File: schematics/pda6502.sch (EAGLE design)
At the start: 32 parts, among them IC1 74HC00D, IC2 74HC138D, IC3 DS1813-SMD, J1 CON_HEADER_2X07-PTH, U1 W65C02S, U2 W65C22S, U3 28C256, U4 UM61256AK-12

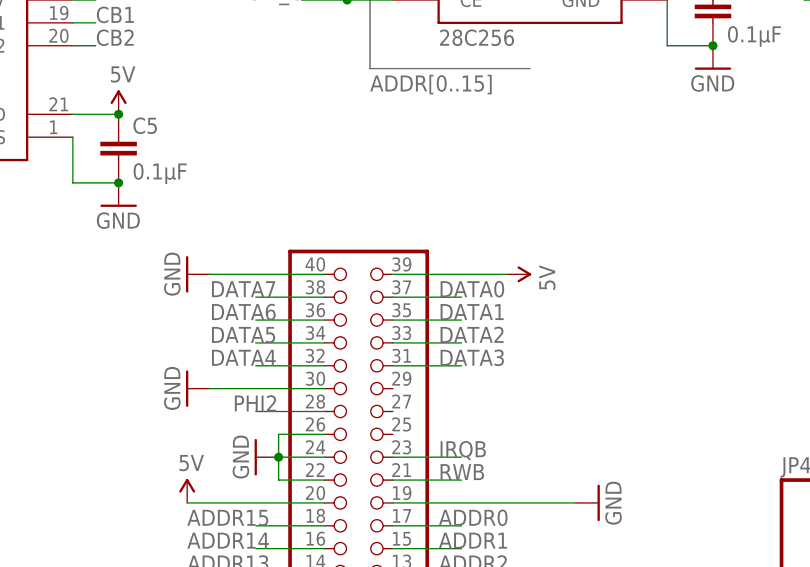
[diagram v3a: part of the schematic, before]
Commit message: schematics: ERC fixes; expansion header has decoupling cap.
(Does the cap even make sense there? The more the merrier...)
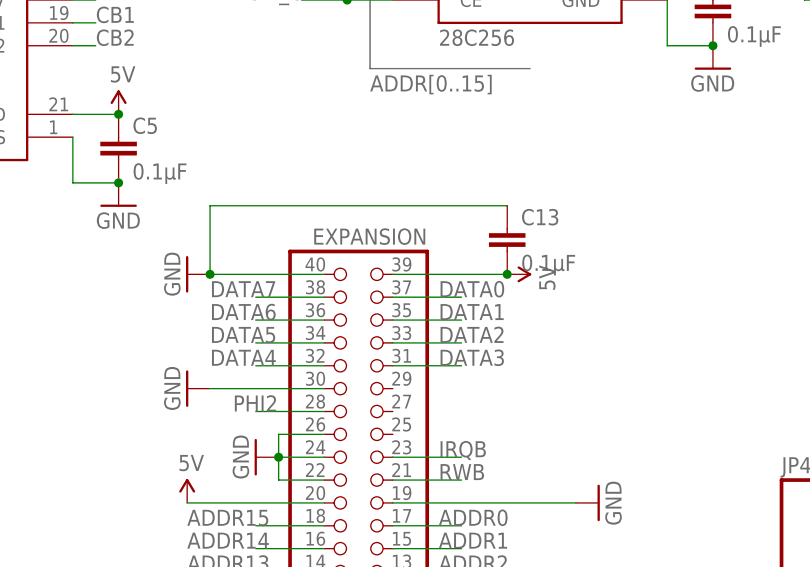
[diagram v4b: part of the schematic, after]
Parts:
- added C13: 0.1μF, rcl:C-EUC0805
- JP6: value (none) -> EXPANSION
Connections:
- net 5V: now also C13.2
- net ADDR1: no longer JP6.19
- net DATA0: now also JP6.37
- net DATA1: now also JP6.35
- net DATA2: now also JP6.33
- net DATA3: now also JP6.31
- net DATA4: now also JP6.32
- net DATA5: now also JP6.34
- net DATA6: now also JP6.36
- net GND: now also C13.1, JP6.19
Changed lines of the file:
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@@
 <part name="JP5" library="SparkFun-Connectors" deviceset="M02" device="PTH" value="EXT5V"/>
 <part name="GND21" library="SparkFun-Aesthetics" deviceset="GND" device=""/>
-<part name="JP6" library="adafruit" deviceset="PINHD-2X20" device=""/>
+<part name="JP6" library="adafruit" deviceset="PINHD-2X20" device="" value="EXPANSION"/>
 <part name="GND17" library="SparkFun-Aesthetics" deviceset="GND" device=""/>
 <part name="GND19" library="SparkFun-Aesthetics" deviceset="GND" device=""/>
@@
 <part name="SUPPLY21" library="SparkFun-Aesthetics" deviceset="5V" device=""/>
 <part name="SUPPLY22" library="SparkFun-Aesthetics" deviceset="5V" device=""/>
+<part name="C13" library="rcl" deviceset="C-EU" device="C0805" value="0.1μF"/>
 </parts>
 <sheets>
@@
 <instance part="SUPPLY21" gate="G$1" x="114.3" y="66.04"/>
 <instance part="SUPPLY22" gate="G$1" x="149.86" y="91.44" rot="R270"/>
+<instance part="C13" gate="G$1" x="149.86" y="96.52"/>
 </instances>
 <busses>
@@
 </segment>
 <segment>
+<pinref part="JP6" gate="A" pin="36"/>
 <wire x1="129.54" y1="86.36" x2="121.92" y2="86.36" width="0.1524" layer="91"/>
 <label x="116.84" y="86.36" size="1.778" layer="95"/>
@@
 </segment>
 <segment>
+<pinref part="JP6" gate="A" pin="34"/>
 <wire x1="129.54" y1="83.82" x2="121.92" y2="83.82" width="0.1524" layer="91"/>
 <label x="116.84" y="83.82" size="1.778" layer="95"/>
@@
 </segment>
 <segment>
+<pinref part="JP6" gate="A" pin="32"/>
 <wire x1="129.54" y1="81.28" x2="121.92" y2="81.28" width="0.1524" layer="91"/>
 <label x="116.84" y="81.28" size="1.778" layer="95"/>
@@
 </segment>
 <segment>
-<wire x1="144.78" y1="81.28" x2="137.16" y2="81.28" width="0.1524" layer="91"/>
+<pinref part="JP6" gate="A" pin="31"/>
+<wire x1="137.16" y1="81.28" x2="144.78" y2="81.28" width="0.1524" layer="91"/>
 <label x="142.24" y="81.28" size="1.778" layer="95"/>
 </segment>
@@
 </segment>
 <segment>
-<wire x1="144.78" y1="83.82" x2="137.16" y2="83.82" width="0.1524" layer="91"/>
+<pinref part="JP6" gate="A" pin="33"/>
+<wire x1="137.16" y1="83.82" x2="144.78" y2="83.82" width="0.1524" layer="91"/>
 <label x="142.24" y="83.82" size="1.778" layer="95"/>
 </segment>
@@
 </segment>
 <segment>
-<wire x1="144.78" y1="86.36" x2="137.16" y2="86.36" width="0.1524" layer="91"/>
+<pinref part="JP6" gate="A" pin="35"/>
+<wire x1="137.16" y1="86.36" x2="144.78" y2="86.36" width="0.1524" layer="91"/>
 <label x="142.24" y="86.36" size="1.778" layer="95"/>
 </segment>
@@
 </segment>
 <segment>
-<wire x1="144.78" y1="88.9" x2="137.16" y2="88.9" width="0.1524" layer="91"/>
+<pinref part="JP6" gate="A" pin="37"/>
+<wire x1="137.16" y1="88.9" x2="144.78" y2="88.9" width="0.1524" layer="91"/>
 <label x="142.24" y="88.9" size="1.778" layer="95"/>
 </segment>
@@
 <pinref part="U3" gate="G$1" pin="A1"/>
 <wire x1="134.62" y1="165.1" x2="137.16" y2="165.1" width="0.1524" layer="91"/>
-</segment>
-<segment>
-<pinref part="JP6" gate="A" pin="19"/>
-<wire x1="137.16" y1="66.04" x2="157.48" y2="66.04" width="0.1524" layer="91"/>
-<pinref part="GND22" gate="1" pin="GND"/>
 </segment>
 <segment>
@@
 <wire x1="129.54" y1="91.44" x2="116.84" y2="91.44" width="0.1524" layer="91"/>
 <pinref part="GND24" gate="1" pin="GND"/>
+<pinref part="C13" gate="G$1" pin="1"/>
+<wire x1="149.86" y1="99.06" x2="116.84" y2="99.06" width="0.1524" layer="91"/>
+<wire x1="116.84" y1="99.06" x2="116.84" y2="91.44" width="0.1524" layer="91"/>
+<junction x="116.84" y="91.44"/>
 </segment>
 <segment>
@@
 <wire x1="129.54" y1="68.58" x2="124.46" y2="68.58" width="0.1524" layer="91"/>
 <pinref part="GND23" gate="1" pin="GND"/>
+</segment>
+<segment>
+<pinref part="JP6" gate="A" pin="19"/>
+<wire x1="137.16" y1="66.04" x2="157.48" y2="66.04" width="0.1524" layer="91"/>
+<pinref part="GND22" gate="1" pin="GND"/>
 </segment>
 </net>
@@
 <pinref part="SUPPLY22" gate="G$1" pin="5V"/>
 <wire x1="137.16" y1="91.44" x2="149.86" y2="91.44" width="0.1524" layer="91"/>
-</segment>
-</net>
+<pinref part="C13" gate="G$1" pin="2"/>
+<junction x="149.86" y="91.44"/>
+</segment>
+</net>

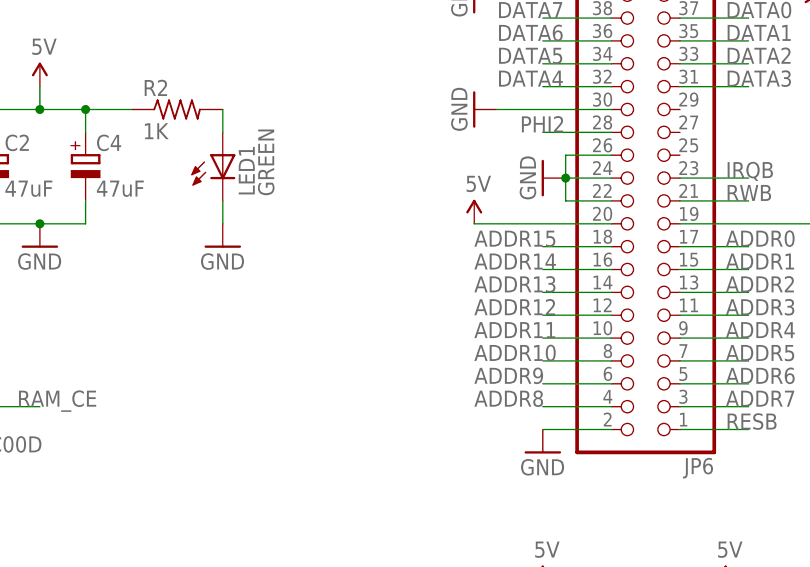
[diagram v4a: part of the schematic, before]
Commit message: schematic, board: added 0.1 uF cap on 5V expansion pin 20.
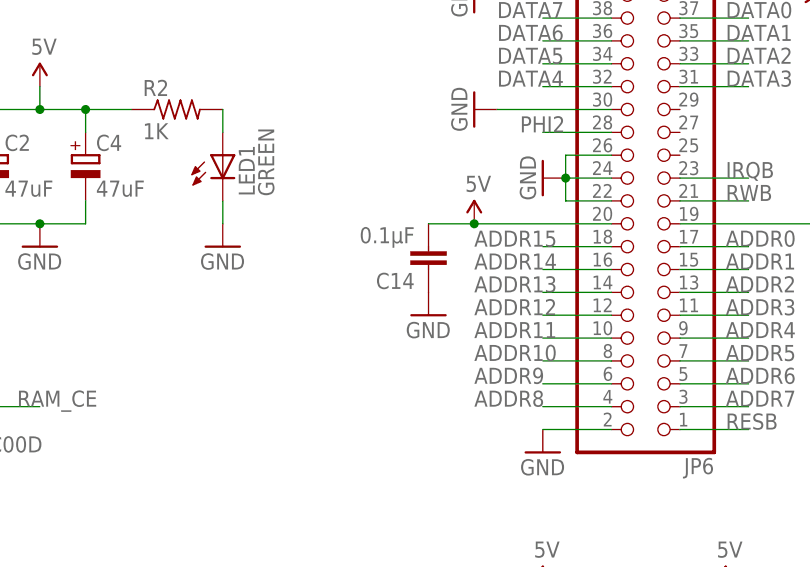
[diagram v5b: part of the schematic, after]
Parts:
- added C14: 0.1μF, rcl:C-EUC0805
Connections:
- net 5V: now also C14.2
- net GND: now also C14.1
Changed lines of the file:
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@@
 <part name="SUPPLY22" library="SparkFun-Aesthetics" deviceset="5V" device=""/>
 <part name="C13" library="rcl" deviceset="C-EU" device="C0805" value="0.1μF"/>
+<part name="C14" library="rcl" deviceset="C-EU" device="C0805" value="0.1μF"/>
+<part name="GND25" library="SparkFun-Aesthetics" deviceset="GND" device=""/>
 </parts>
 <sheets>
@@
 <instance part="SUPPLY22" gate="G$1" x="149.86" y="91.44" rot="R270"/>
 <instance part="C13" gate="G$1" x="149.86" y="96.52"/>
+<instance part="C14" gate="G$1" x="109.22" y="60.96" rot="R180"/>
+<instance part="GND25" gate="1" x="109.22" y="55.88"/>
 </instances>
 <busses>
@@
 <wire x1="137.16" y1="66.04" x2="157.48" y2="66.04" width="0.1524" layer="91"/>
 <pinref part="GND22" gate="1" pin="GND"/>
+</segment>
+<segment>
+<pinref part="C14" gate="G$1" pin="1"/>
+<pinref part="GND25" gate="1" pin="GND"/>
 </segment>
 </net>
@@
 <pinref part="JP6" gate="A" pin="20"/>
 <wire x1="114.3" y1="66.04" x2="129.54" y2="66.04" width="0.1524" layer="91"/>
-</segment>
-<segment>
+<pinref part="C14" gate="G$1" pin="2"/>
+<wire x1="114.3" y1="66.04" x2="109.22" y2="66.04" width="0.1524" layer="91"/>
+<junction x="114.3" y="66.04"/>
+</segment>
+<segment>

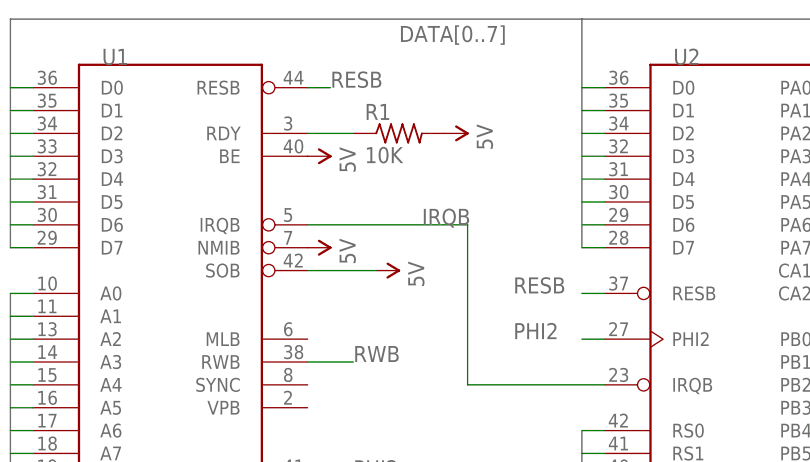
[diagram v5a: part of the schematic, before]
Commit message: schematics, board: resistor on BE. routing tweaks.
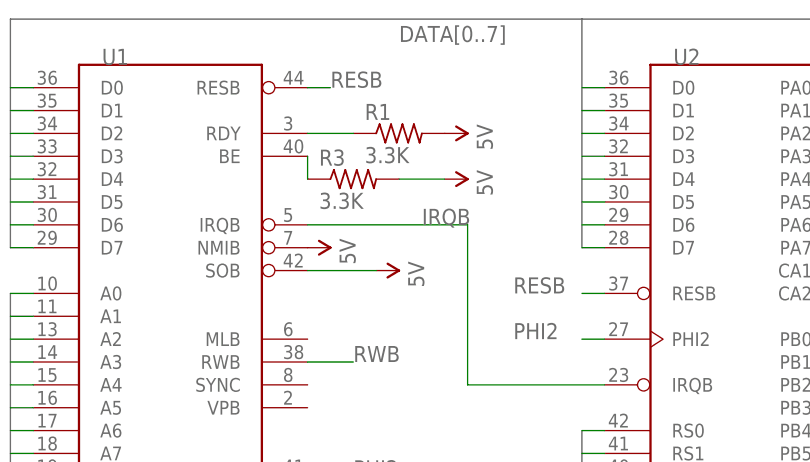
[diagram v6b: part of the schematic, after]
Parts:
- added R3: 3.3K, resistor:R-US_R0805
- R1: value 10K -> 3.3K
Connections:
- new net N$8: R3.1, U1.BE
- net 5V: now also R3.2; no longer U1.BE
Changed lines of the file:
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@@
 <part name="SUPPLY2" library="SparkFun-Aesthetics" deviceset="5V" device=""/>
 <part name="SUPPLY1" library="SparkFun-Aesthetics" deviceset="5V" device=""/>
-<part name="R1" library="resistor" deviceset="R-US_" device="R0805" value="10K"/>
+<part name="R1" library="resistor" deviceset="R-US_" device="R0805" value="3.3K"/>
 <part name="SUPPLY6" library="SparkFun-Aesthetics" deviceset="5V" device=""/>
 <part name="J1" library="dangerousprototypes_devices" deviceset="CON_HEADER_2X07" device="-PTH"/>
@@
 <part name="C14" library="rcl" deviceset="C-EU" device="C0805" value="0.1μF"/>
 <part name="GND25" library="SparkFun-Aesthetics" deviceset="GND" device=""/>
+<part name="R3" library="resistor" deviceset="R-US_" device="R0805" value="3.3K"/>
 </parts>
 <sheets>
@@
 <instance part="SUPPLY4" gate="G$1" x="45.72" y="147.32" rot="R270"/>
 <instance part="SUPPLY2" gate="G$1" x="38.1" y="149.86" rot="R270"/>
-<instance part="SUPPLY1" gate="G$1" x="38.1" y="160.02" rot="R270"/>
+<instance part="SUPPLY1" gate="G$1" x="53.34" y="157.48" rot="R270"/>
 <instance part="R1" gate="G$1" x="48.26" y="162.56"/>
 <instance part="SUPPLY6" gate="G$1" x="53.34" y="162.56" rot="R270"/>
@@
 <instance part="C14" gate="G$1" x="109.22" y="60.96" rot="R180"/>
 <instance part="GND25" gate="1" x="109.22" y="55.88"/>
+<instance part="R3" gate="G$1" x="43.18" y="157.48"/>
 </instances>
 <busses>
@@
 </segment>
 <segment>
-<pinref part="U1" gate="G$1" pin="BE"/>
-<pinref part="SUPPLY1" gate="G$1" pin="5V"/>
-</segment>
-<segment>
 <pinref part="R1" gate="G$1" pin="2"/>
 <pinref part="SUPPLY6" gate="G$1" pin="5V"/>
@@
 <pinref part="C13" gate="G$1" pin="2"/>
 <junction x="149.86" y="91.44"/>
+</segment>
+<segment>
+<pinref part="R3" gate="G$1" pin="2"/>
+<pinref part="SUPPLY1" gate="G$1" pin="5V"/>
+<wire x1="48.26" y1="157.48" x2="53.34" y2="157.48" width="0.1524" layer="91"/>
 </segment>
 </net>
@@
 </segment>
 </net>
+<net name="N$8" class="0">
+<segment>
+<pinref part="U1" gate="G$1" pin="BE"/>
+<pinref part="R3" gate="G$1" pin="1"/>
+<wire x1="38.1" y1="160.02" x2="38.1" y2="157.48" width="0.1524" layer="91"/>
+</segment>
+</net>
